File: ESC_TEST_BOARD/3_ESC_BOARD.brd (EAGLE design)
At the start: 61.6 x 68.1 mm, 34 parts

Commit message: Finshing out circuit board
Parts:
- added BOOT: (no value), DiscreteComponents:SW_2512
- added C11, C12, C13, C14, C15, C16, C17: (no value), rcl:C0603
- added C18, C19, C20: (no value), PowerComponents:CPOL-US(10.3_10.3MM)
- added C21, C22, C23: 0.1uF, SparkFun-Capacitors:0603
- added J3: AVR_SPI_PROG_3X2NS, SparkFun-Connectors:2X3-NS
- added JP1, JP10, JP11, JP12, JP13, JP14, JP15, JP2, JP3, JP4, JP5, JP6, JP7, JP8, JP9: (no value), pinhead:1X01
- added R10, R11, R12: (no value), SparkFun-Resistors:0603
- added U2: ATMEGA328P_TQFP, SparkFun-IC-Microcontroller:TQFP32-08
- added Y2: (no value), SparkFun-Clocks:HC49US
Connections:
- removed net CLK: U$4.CLK
- removed net CS/SHDN: U$4.CS/SHDN
- removed net DIN: U$4.DIN
- removed net DOUT: U$4.DOUT
- new net CS: TO-MICRO.4, U$4.CS/SHDN, U2.14
- new net IN: U2.31
- new net MISO: J3.1, TO-MICRO.2, U$4.DOUT, U2.16
- new net MOSI: J3.4, TO-MICRO.3, U$4.DIN, U2.15
- new net N$14: C16.1, U2.7, Y2.2
- new net N$15: C17.1, U2.8, Y2.1
- new net N$24: JP9.1
- new net N$25: JP10.1
- new net RESET: BOOT.2, C11.2, J3.5, R10.1, U2.29
- new net SCK: J3.3, TO-MICRO.1, U$4.CLK, U2.17
- new net SCL: JP8.1, R11.1, U2.28
- new net SDA: JP7.1, R12.1, U2.27
- net +12V: now also JP13.1
- net +5V: now also C12.1, C13.1, C14.1, C15.1, J3.2, JP11.1, JP12.1, R10.2, R11.2, R12.2, U2.18, U2.20, U2.4, U2.6
- net ANALOG_1: now also JP1.1
- net ANALOG_2: now also JP2.1
- net ANALOG_3: now also JP3.1
- net ANALOG_4: now also JP4.1
- net ANALOG_5: now also JP5.1
- net ANALOG_6: now also JP6.1
- net ESC1: now also C18.+, C21.1
- net ESC2: now also C19.+, C22.1
- net ESC3: now also C20.+, C23.1
- net GND: now also BOOT.1, C11.1, C12.2, C13.2, C14.2, C15.2, C16.2, C17.2, C18.-, C19.-, C20.-, C21.2, C22.2, C23.2, J3.6, JP14.1, JP15.1, U2.21, U2.3, U2.5

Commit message: Removed backup files, moved parts
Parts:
- moved C21 622.9 mm to (101.4, 15.9)
- moved C22 622.9 mm to (101.4, 12.6)
- moved JP14 622.9 mm to (106.4, 40.5)
- moved JP15 622.9 mm to (106.4, 25.2)
- moved R11 622.9 mm to (101.4, 6.00)
- moved R12 622.9 mm to (101.4, 2.70)
- moved C23 622.9 mm to (101.4, 9.30)
- moved JP13 622.9 mm to (106.4, 55.8)
- moved JP12 552.9 mm to (29.3, 15.0)
- moved JP11 550.0 mm to (21.6, 28.4)
- moved JP10 523.8 mm to (25.5, 16.8)
- moved JP8 505.8 mm to (26.4, 29.1)
- moved JP9 503.4 mm to (22.6, 11.9)
- moved JP7 499.9 mm to (31.2, 37.7)
- moved JP6 483.3 mm to (28.3, 36.6)
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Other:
- board size 61.6 x 68.1 mm -> 119.2 x 68.1 mm

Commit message: Saving before autoroute
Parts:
- moved ESC2_CON 91.2 mm to (4.30, 33.8), turned to 270 degrees
- moved ESC3_CON 76.4 mm to (4.40, 57.9), turned to 270 degrees
- moved TO-MICRO 65.3 mm to (84.6, 62.3)
- moved C11 59.3 mm to (84.7, 40.3), turned to 270 degrees
- moved U$3 58.7 mm to (69.3, 58.8)
- moved C18 54.3 mm to (59.3, 11.5)
- moved PWM_HEADER 50.0 mm to (72.4, 63.9), turned to 180 degrees
- moved C7 48.8 mm to (69.4, 44.0)
- moved U$4 48.7 mm to (83.9, 54.1)
- moved C12 48.3 mm to (82.3, 11.4)
- moved C17 47.3 mm to (73.7, 26.2), turned to 270 degrees
- moved Y2 44.2 mm to (78.2, 29.5), turned to 90 degrees
- moved R12 39.6 mm to (88.6, 40.2), turned to 90 degrees
- moved J2 38.7 mm to (107.1, 4.34)
- moved R10 37.7 mm to (81.2, 7.40), turned to 90 degrees
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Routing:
- added copper zone on layer 1, net GND

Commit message: Updating ESC Test Board
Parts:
- removed JP10, JP11, JP15, JP9: (no value), pinhead:1X01
- removed TO-MICRO: (no value), con-lstb:MA04-1
- moved JP8 94.5 mm to (116.8, 1.67)
- moved JP6 94.3 mm to (117.1, 4.85)
- moved JP1 91.7 mm to (116.8, 12.2)
- moved JP7 90.5 mm to (116.8, 8.24)
- moved JP12 88.1 mm to (117.2, 21.4)
- moved C23 67.8 mm to (64.3, 66.1), turned to 90 degrees
- moved PWM_HEADER 63.6 mm to (57.7, 2.03), turned to 0 degrees
- moved R2 57.4 mm to (64.6, 8.74), turned to 270 degrees
- moved C10 55.8 mm to (80.5, 44.3), flipped to the bottom, turned to 180 degrees
- moved U$1 51.4 mm to (65.2, 14.6), turned to 270 degrees
- moved U$2 48.5 mm to (65.2, 37.6), turned to 270 degrees
- moved C22 48.1 mm to (64.3, 43.3), turned to 90 degrees
- moved C6 45.2 mm to (67.1, 54.2), turned to 270 degrees
- moved R1 44.0 mm to (64.6, 31.6), turned to 270 degrees
- moved R5 43.8 mm to (29.3, 57.7), flipped to the bottom, turned to 180 degrees
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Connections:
- removed net IN: U2.31
- removed net N$24: JP9.1
- removed net N$25: JP10.1
- net +5V: no longer JP11.1
- net CS: no longer TO-MICRO.4
- net GND: no longer JP15.1
- net MISO: no longer TO-MICRO.2
- net MOSI: no longer TO-MICRO.3
- net SCK: no longer TO-MICRO.1
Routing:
- net N$9: track 0.00 -> 7.93 mm
- net N$5: track 0.00 -> 7.92 mm
- net N$12: track 0.00 -> 7.86 mm
- net N$10: track 0.00 -> 7.85 mm
- net N$1: track 0.00 -> 7.79 mm
- net N$7: track 0.00 -> 7.78 mm
- net N$8: track 0.00 -> 7.14 mm
- net N$3: track 0.00 -> 7.12 mm
- net N$11: track 0.00 -> 7.06 mm
- net +5V: track 0.00 -> 6.89 mm
- net N$4: track 0.00 -> 2.36 mm
- net N$6: track 0.00 -> 2.26 mm
- net N$2: track 0.00 -> 2.24 mm
- net ANALOG_4: track 0.00 -> 1.85 mm
- net ANALOG_5: track 0.00 -> 1.83 mm
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- added copper zone on layer 1, net +12V

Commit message: Updating ESC Test Board
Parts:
- removed BOOT: (no value), DiscreteComponents:SW_2512
- removed JP7, JP8: (no value), pinhead:1X01
- added RESET: (no value), DiscreteComponents:SW_2512
- added SV2: (no value), con-lsta:FE06-2
- moved J2 58.8 mm to (73.8, 62.1), turned to 90 degrees
- moved J1 58.7 mm to (81.4, 61.9), turned to 90 degrees
- moved J3 56.1 mm to (99.6, 7.23)
- moved C1 36.8 mm to (102.2, 51.3), flipped to the top, turned to 270 degrees
- moved C2 36.7 mm to (100.3, 51.3), flipped to the top, turned to 270 degrees
- moved C3 36.5 mm to (98.4, 51.3), flipped to the top, turned to 270 degrees
- moved C7 36.4 mm to (96.4, 51.3), flipped to the top, turned to 90 degrees
- moved C8 36.3 mm to (94.5, 51.3), flipped to the top, turned to 90 degrees
- moved C9 36.3 mm to (92.6, 51.3), flipped to the top, turned to 90 degrees
- moved C16 28.7 mm to (108.6, 24.6), flipped to the bottom, turned to 270 degrees
- moved R12 26.8 mm to (111.8, 14.0), turned to 0 degrees
- moved R11 24.9 mm to (111.8, 15.6), turned to 0 degrees
- moved U$4 23.4 mm to (97.4, 43.0), flipped to the top, turned to 180 degrees
- moved R10 23.2 mm to (111.8, 17.2), turned to 0 degrees
- moved Y2 22.7 mm to (102.4, 25.5), turned to 0 degrees
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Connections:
- new net +3V3: R11.2, R12.2
- new net PB0: SV2.6, U2.12
- new net PD3: SV2.1, U2.1
- new net PD4: SV2.2, U2.2
- new net PD5: SV2.3, U2.9
- new net PD6: SV2.4, U2.10
- new net PD7: SV2.5, U2.11
- net +5V: no longer R11.2, R12.2
- net CS: now also SV2.7
- net GND: now also RESET.1; no longer BOOT.1
- net MISO: now also SV2.9
- net MOSI: now also SV2.8
- net RESET: now also RESET.2; no longer BOOT.2
- net SCK: now also SV2.10
- net SCL: now also SV2.12; no longer JP8.1
- net SDA: now also SV2.11; no longer JP7.1
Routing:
- net ANALOG_4: track 1.85 -> 5.25 mm, vias 0 -> 1
- net ANALOG_5: track 1.83 -> 0.00 mm
- net ANALOG_6: track 1.81 -> 0.00 mm
- added copper zone on layer 16, net +12V
- added copper zone on layer 1, net ESC1
- added copper zone on layer 1, net ESC2
- added copper zone on layer 1, net ESC3

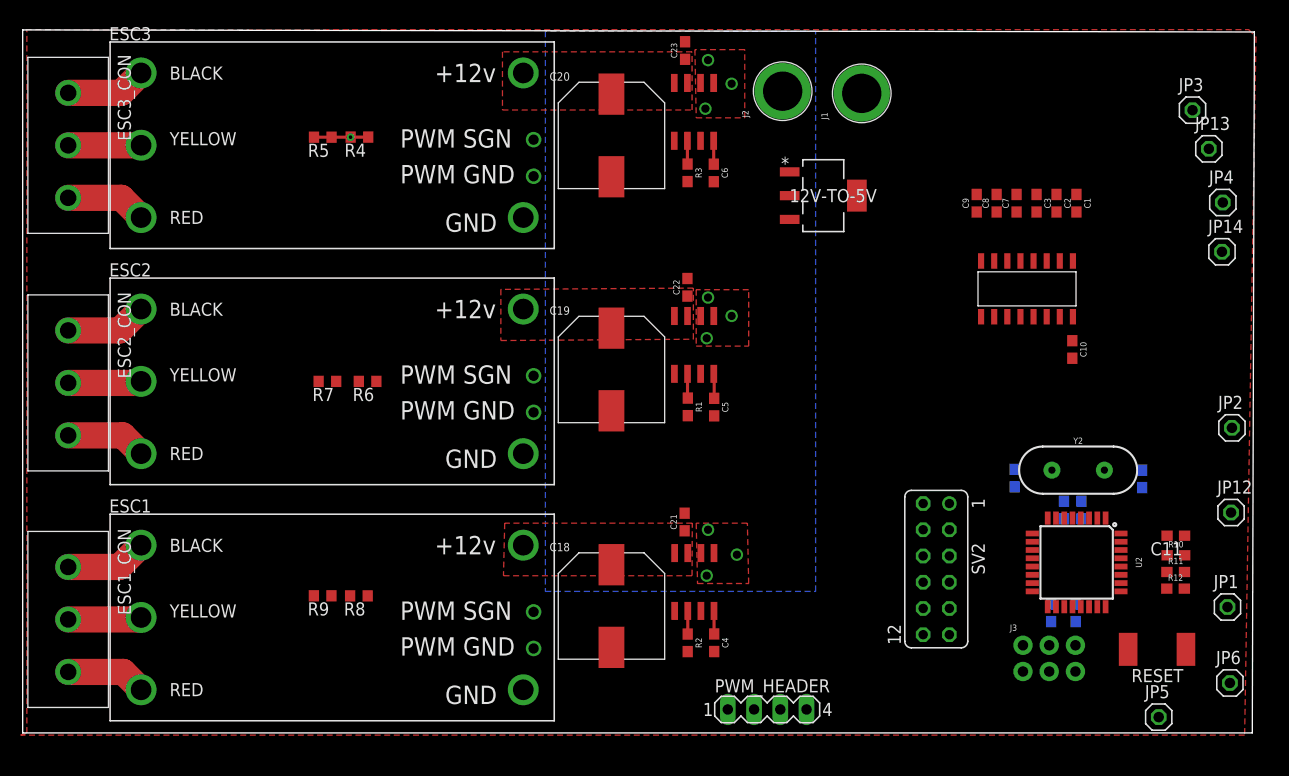
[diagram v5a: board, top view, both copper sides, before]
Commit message: Almost done with initial routing
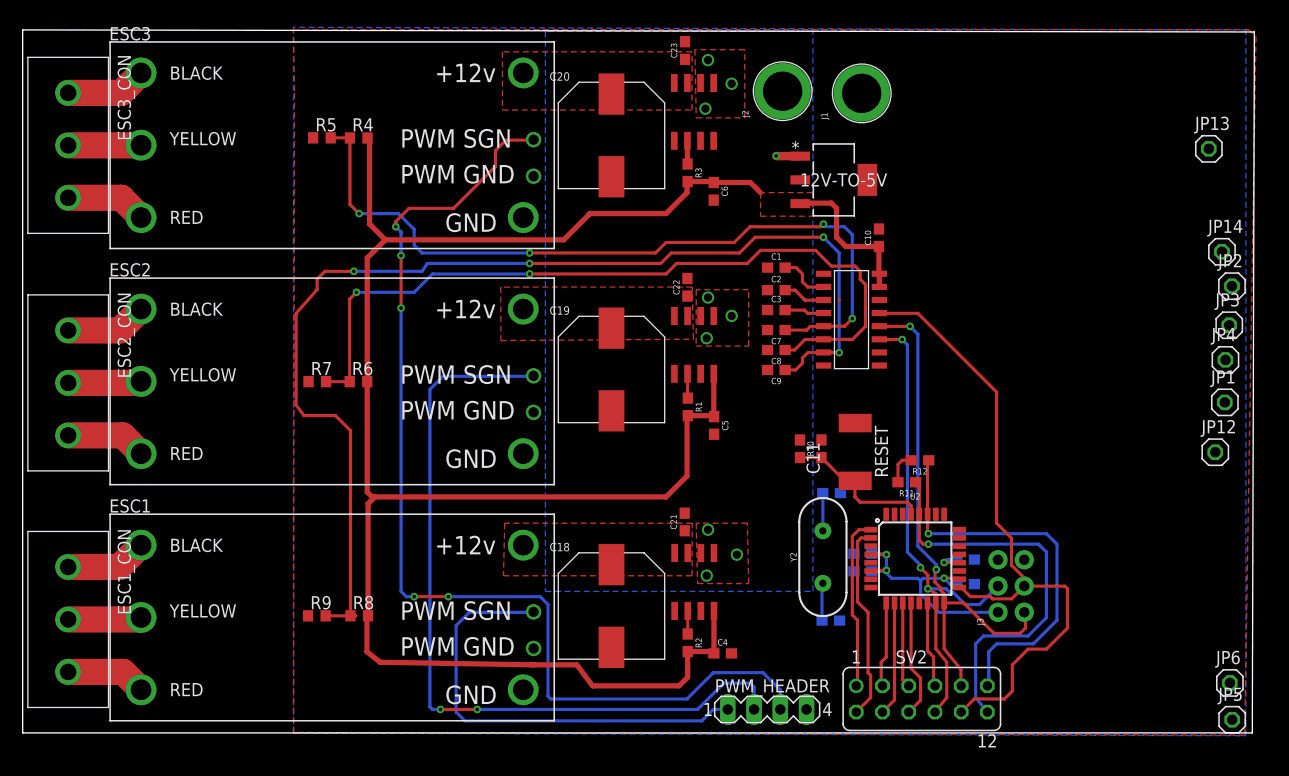
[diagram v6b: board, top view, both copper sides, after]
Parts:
- moved C11 37.3 mm to (75.5, 27.5), turned to 270 degrees
- moved R10 35.8 mm to (77.5, 27.5), turned to 90 degrees
- moved RESET 34.9 mm to (80.8, 27.2), turned to 270 degrees
- moved C16 30.1 mm to (78.5, 23.2), turned to 180 degrees
- moved C1 29.7 mm to (73.2, 45.1), turned to 0 degrees
- moved C2 28.4 mm to (73.2, 42.9), turned to 0 degrees
- moved R12 27.7 mm to (87.1, 26.4), turned to 180 degrees
- moved R11 27.4 mm to (85.8, 24.3), turned to 180 degrees
- moved C3 27.2 mm to (73.2, 40.9), turned to 0 degrees
- moved C7 26.3 mm to (73.2, 39.0), turned to 180 degrees
- moved Y2 26.1 mm to (77.7, 17.0), turned to 90 degrees
- moved C8 25.6 mm to (73.2, 37.1), turned to 180 degrees
- moved C9 25.2 mm to (73.2, 35.2), turned to 180 degrees
- moved C17 22.5 mm to (78.4, 10.9), turned to 180 degrees
- moved C10 21.6 mm to (83.1, 48.0), turned to 90 degrees
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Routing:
- net +5V: track 6.89 -> 222.2 mm, vias 0 -> 4
- net ANALOG_6: track 0.00 -> 109.5 mm, vias 0 -> 4
- net PWM3: track 0.00 -> 103.4 mm, vias 0 -> 5
- net ANALOG_5: track 0.00 -> 76.8 mm, vias 0 -> 2
- net PWM2: track 0.00 -> 76.2 mm, vias 0 -> 2
- net ANALOG_4: track 5.25 -> 76.5 mm, vias 1 -> 4
- net SCK: track 0.00 -> 64.9 mm
- net MISO: track 0.00 -> 50.7 mm, vias 0 -> 2
- net MOSI: track 0.00 -> 48.7 mm, vias 0 -> 3
- net PWM1: track 0.00 -> 43.5 mm
- net SCL: track 0.00 -> 39.8 mm, vias 0 -> 1
- net SDA: track 0.00 -> 38.6 mm, vias 0 -> 1
- net PD4: track 0.00 -> 19.0 mm
- net PD3: track 0.00 -> 16.8 mm
- net RESET: track 0.00 -> 14.5 mm
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- added copper zone on layer 1, net +5V
- added copper zone on layer 16, net GND

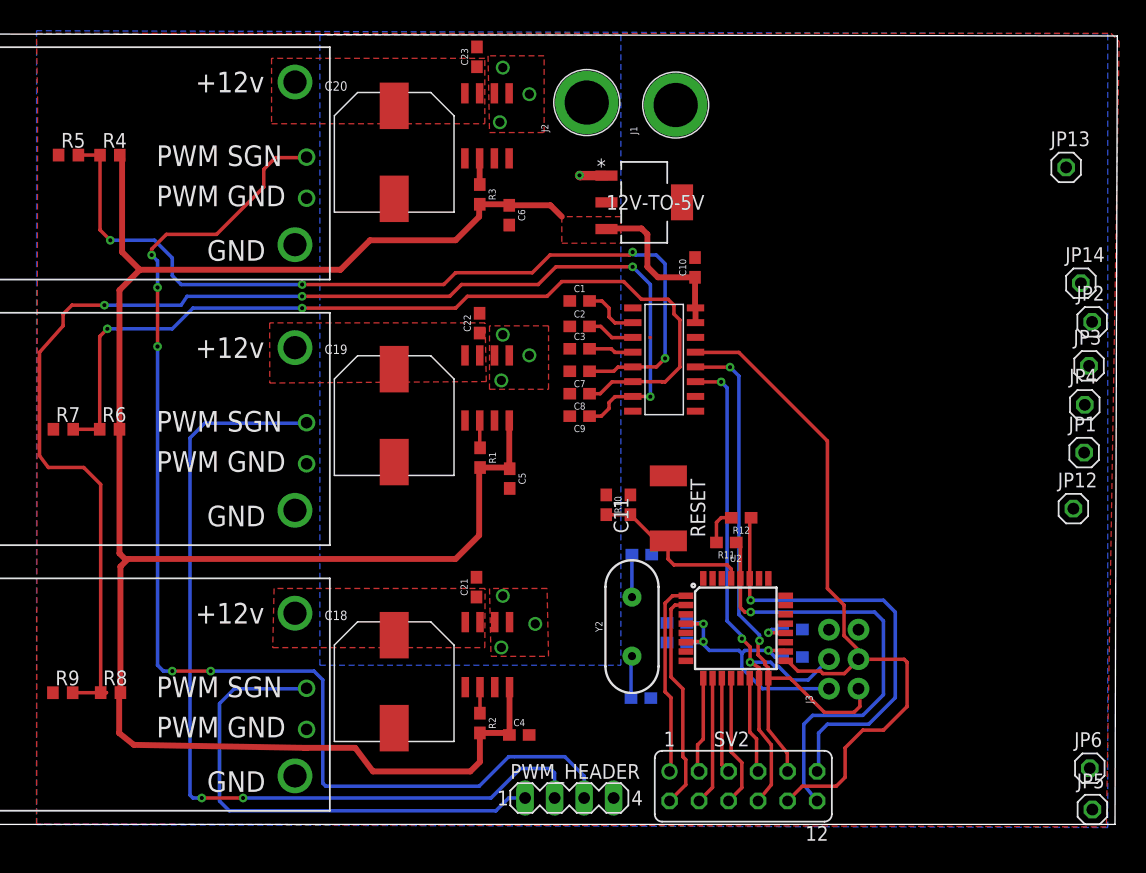
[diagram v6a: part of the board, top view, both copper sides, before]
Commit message: Finished routing of Jacobs section
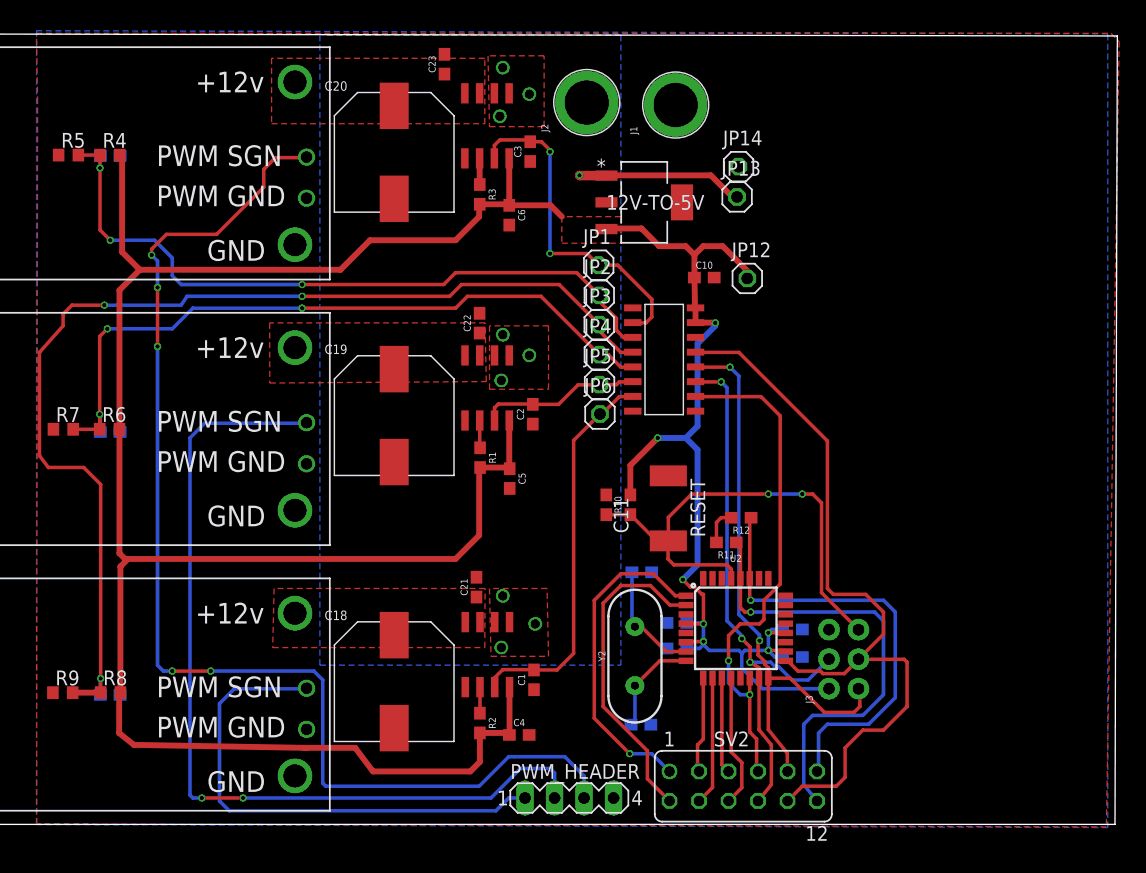
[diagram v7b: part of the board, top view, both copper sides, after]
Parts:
- moved JP5 56.0 mm to (74.9, 37.9)
- moved JP6 52.0 mm to (74.9, 35.3)
- moved C9 47.0 mm to (32.8, 11.2), flipped to the bottom
- moved JP1 44.8 mm to (74.8, 48.1)
- moved C7 44.5 mm to (32.8, 57.6), flipped to the bottom
- moved JP2 42.5 mm to (74.9, 45.6)
- moved JP3 42.3 mm to (74.8, 43.0)
- moved JP4 42.0 mm to (74.9, 40.4)
- moved C8 40.5 mm to (32.8, 33.8), flipped to the bottom
- moved JP12 34.4 mm to (87.6, 47.0)
- moved C1 32.8 mm to (69.2, 12.5), turned to 90 degrees
- moved JP14 31.1 mm to (86.8, 56.6)
- moved JP13 28.4 mm to (86.7, 54.0)
- moved C3 17.5 mm to (68.9, 57.9), turned to 90 degrees
- moved C2 8.57 mm to (69.1, 35.3), turned to 90 degrees
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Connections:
- net ANALOG_1: now also C3.2, U$3.VIOUT; no longer C1.2, U$1.VIOUT
- net ANALOG_2: now also C7.1, R4.1, R5.2; no longer C2.2, U$2.VIOUT
- net ANALOG_3: now also C9.1, R8.1, R9.2; no longer C3.2, U$3.VIOUT
- net ANALOG_4: now also C8.1, R6.1, R7.2; no longer C7.1, R4.1, R5.2
- net ANALOG_5: now also C2.2, U$2.VIOUT; no longer C8.1, R6.1, R7.2
- net ANALOG_6: now also C1.2, U$1.VIOUT; no longer C9.1, R8.1, R9.2
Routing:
- net ANALOG_3: track 3.86 -> 94.0 mm, vias 0 -> 3
- net ANALOG_6: track 109.5 -> 33.6 mm, vias 4 -> 0
- net ANALOG_5: track 76.8 -> 14.1 mm, vias 2 -> 0
- net ANALOG_2: track 4.17 -> 61.7 mm, vias 0 -> 3
- net +5V: track 222.2 -> 272.7 mm, vias 4 -> 7
- net CS: track 8.32 -> 44.3 mm, vias 0 -> 2
- net RESET: track 14.5 -> 43.0 mm, vias 0 -> 2
- net ANALOG_1: track 4.96 -> 29.2 mm, vias 0 -> 2
- net ANALOG_4: track 76.5 -> 61.7 mm, vias 4 -> 3
- net +12V: track 2.33 -> 14.4 mm
- net PD3: track 16.8 -> 28.2 mm, vias 0 -> 1
- net PD4: track 19.0 -> 27.8 mm
- net N$14: track 3.66 -> 10.1 mm
- net N$15: track 3.64 -> 8.77 mm
- net SCK: track 64.9 -> 68.3 mm
